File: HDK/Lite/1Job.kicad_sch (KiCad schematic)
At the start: 7 parts, among them U101 STM32G030K6Tx, U102 AMS1117-3.3

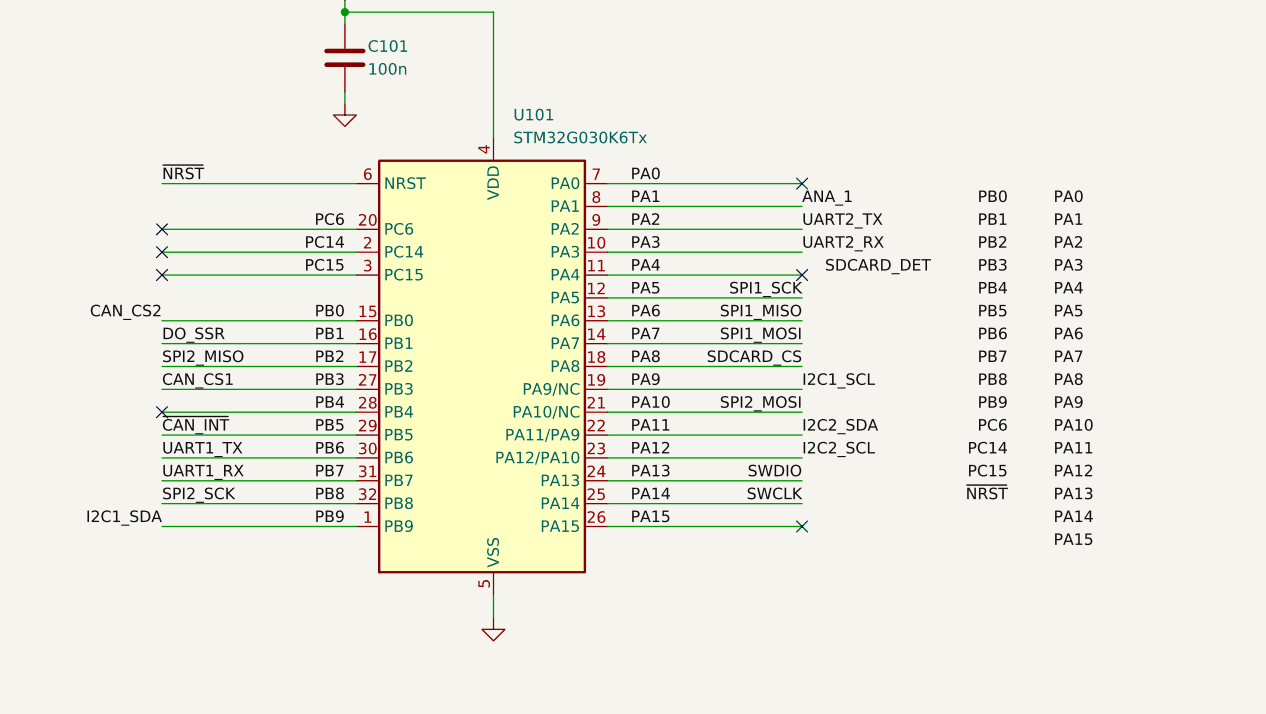
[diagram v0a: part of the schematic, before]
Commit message: updated 1Job, 75%
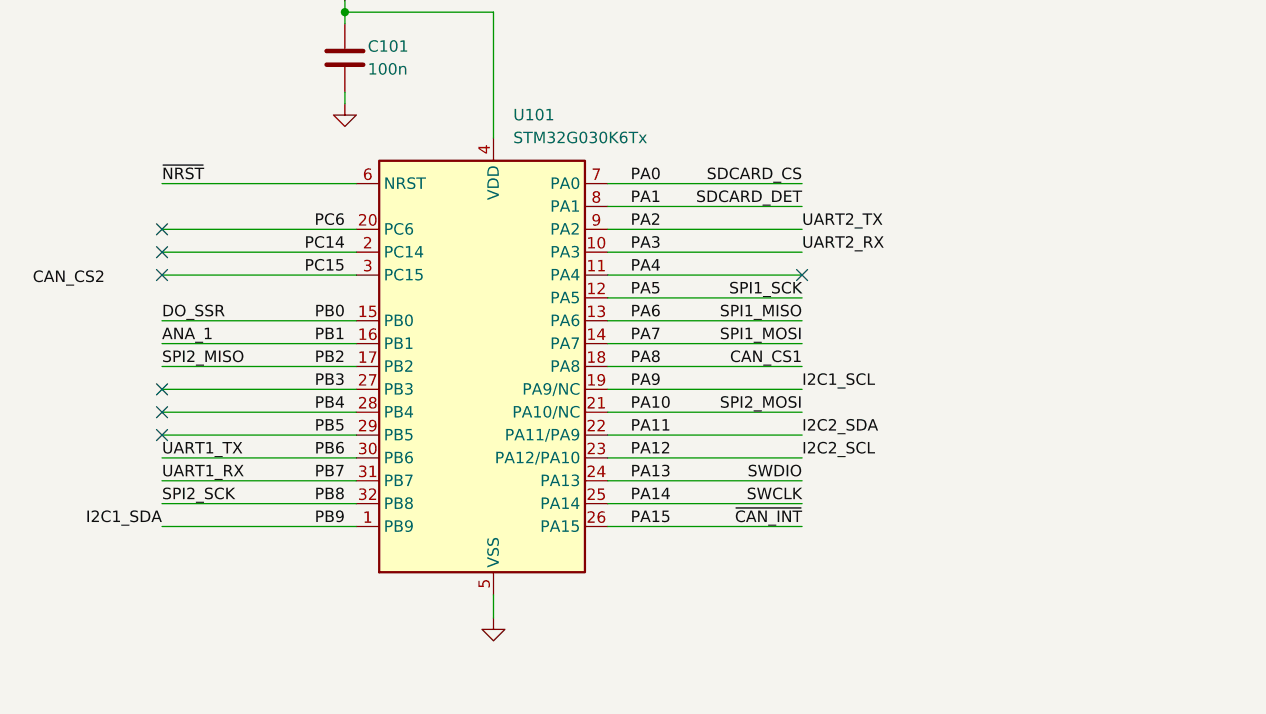
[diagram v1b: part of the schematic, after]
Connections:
- net PA8 is gone; now on net CAN_CS1: U101.18 (PA8)
- net ANA_1: now also U101.16 (PB1); no longer U101.8 (PA1)
- net CAN_CS1: no longer U101.27 (PB3)
- net CAN_CS2: no longer U101.15 (PB0)
- net DO_SSR: now also U101.15 (PB0); no longer U101.16 (PB1)
- new net PA1: U101.8 (PA1)
- new net PB3: U101.27 (PB3)

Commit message: updated 1 Job, 85%
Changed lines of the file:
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@@
     (effects (font (size 1.27 1.27)) (justify left bottom))
-  )
-  (label "CAN_CS2" (at 26.67 60.96 180) (fields_autoplaced)
-    (effects (font (size 1.27 1.27)) (justify right bottom))
   )
   (label "CAN_+" (at 199.39 93.98 0) (fields_autoplaced)

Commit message: updated 1-Job, v1rA
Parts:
- added D101, D102: LED, LED_SMD:LED_0603_1608Metric, symbol Device:LED
- added R201 (x2): 10k, Resistor_SMD:R_0603_1608Metric, symbol Device:R
- C101, C103, C105: LCSC (none) -> C57112
- C102, C104: LCSC (none) -> C28323
- U101: LCSC (none) -> C724043
- U102: LCSC (none) -> C6186
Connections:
- net +3V3: now also R201.2, R201.2
- net GND: now also D102.1 (K)
- net PA4: now also D101.1 (K)
- new net: D102.2 (A), R201.1
- new net: D101.2 (A), R201.1
- no-connect marks 9 -> 6
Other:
- sheet 1JIO ports: added I2C1_SCL, I2C1_SDA, I2C2_SCL, I2C2_SDA, PB3, PB4, PB5, SPI1_MISO, SPI1_MOSI, SPI1_SCK, SPI2_MISO, SPI2_MOSI, SPI2_SCK, UART2_RX, UART2_TX, ~{NRST}; removed none

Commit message: updated 1job silkscreen
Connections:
- no-connect marks 6 -> 5
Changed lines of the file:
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@@
   )
   (no_connect (at 199.39 43.18))
-  (no_connect (at 104.14 59.69))
   (no_connect (at 33.02 57.15))
   (no_connect (at 33.02 54.61))
@@
     (effects (font (size 1.27 1.27)) (justify left bottom))
   )
+  (label "USR_LED" (at 104.14 59.69 180) (fields_autoplaced)
+    (effects (font (size 1.27 1.27)) (justify right bottom))
+  )
   (label "PA15" (at 85.09 87.63 0) (fields_autoplaced)
     (effects (font (size 1.27 1.27)) (justify left bottom))
@@
     (effects (font (size 1.27 1.27)) (justify right bottom))
   )
+  (label "USR_LED" (at 78.74 176.53 180) (fields_autoplaced)
+    (effects (font (size 1.27 1.27)) (justify right bottom))
+  )
   (label "SPI1_SCK" (at 199.39 57.15 0) (fields_autoplaced)
     (effects (font (size 1.27 1.27)) (justify left bottom))
@@
     (effects (font (size 1.27 1.27)) (justify right bottom))
   )
-  (label "PA4" (at 78.74 176.53 180) (fields_autoplaced)
-    (effects (font (size 1.27 1.27)) (justify right bottom))
-  )

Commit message: updated 1job
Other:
- company: (none) -> Scott CJX
- title: (none) -> 1 Job Lite
- moved on the sheet: C102, C103, C104, C105, D101, D102, R201, U102
